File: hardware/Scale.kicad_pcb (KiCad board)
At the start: 2 copper layers, 45 x 45 mm, 158 parts, among them J1 Load Cell Connector, J2 GPIO, J3 RS232, J4 DebugEdge_02x03, J5 Display Connector, J7 12401610E4#2A, Q1 DMG2307L, Q2 DMG2307L, Q3 BSD235N, SW1 RESET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

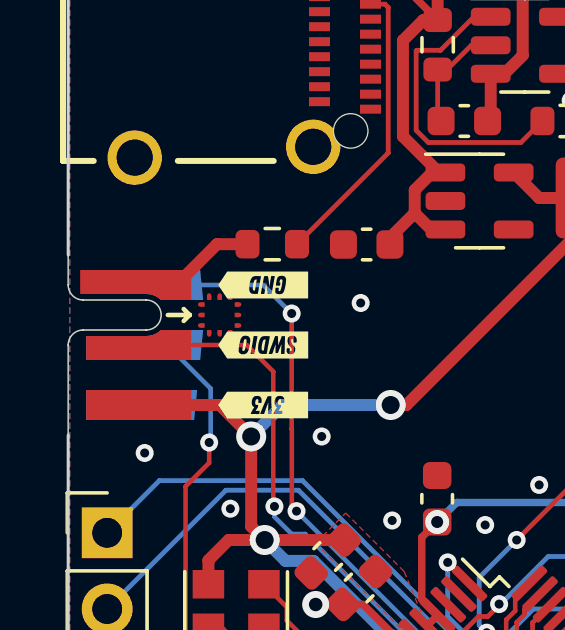
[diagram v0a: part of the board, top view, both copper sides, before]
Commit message: Fixed encoder and usb 3D models
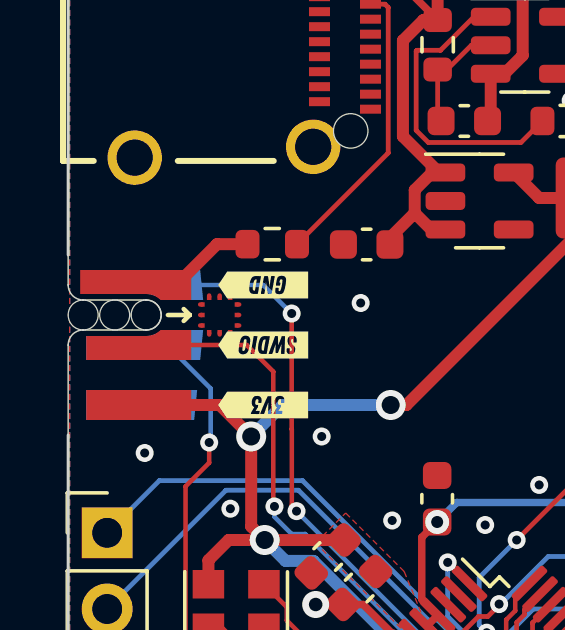
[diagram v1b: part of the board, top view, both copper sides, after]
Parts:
- added REF**: NPTH, PCM_kikit:NPTH, F.Cu at (115.8, 62.6)
- added REF**: NPTH, PCM_kikit:NPTH, F.Cu at (114.8, 62.6)
- added REF**: NPTH, PCM_kikit:NPTH, F.Cu at (113.8, 62.6)
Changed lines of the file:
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@@
 		)
 	)
+	(footprint "PCM_kikit:NPTH"
+		(layer "F.Cu")
+		(at 115.85 62.65)
+		(property "Reference" "REF**"
+			(at 0 0.5 0)
+			(layer "F.SilkS")
+			(hide yes)
+			(effects
+				(font
+					(size 1 1)
+					(thickness 0.15)
+				)
+			)
+		)
+		(property "Value" "NPTH"
+			(at 0 -0.5 0)
+			(layer "F.Fab")
+			(hide yes)
+			(effects
+				(font
+					(size 1 1)
+					(thickness 0.15)
+				)
+			)
+		)
+		(property "Datasheet" ""
+			(at 0 0 0)
+			(layer "F.Fab")
+			(hide yes)
+			(effects
+				(font
+					(size 1.27 1.27)
+					(thickness 0.15)
+				)
+			)
+		)
+		(property "Description" ""
+			(at 0 0 0)
+			(layer "F.Fab")
+			(hide yes)
+			(effects
+				(font
+					(size 1.27 1.27)
+					(thickness 0.15)
+				)
+			)
+		)
+		(attr through_hole)
+		(pad "" np_thru_hole circle
+			(at 0 0)
+			(size 1 1)
+			(drill 1)
+			(layers "*.Mask")
+		)
+		(embedded_fonts no)
+	)
 	(footprint "Resistor_SMD:R_0603_1608Metric"
 		(placed yes)
@@
 		)
 	)
+	(footprint "PCM_kikit:NPTH"
+		(layer "F.Cu")
+		(at 114.8 62.65)
+		(property "Reference" "REF**"
+			(at 0 0.5 0)
+			(layer "F.SilkS")
+			(hide yes)
+			(effects
+				(font
+					(size 1 1)
+					(thickness 0.15)
+				)
+			)
+		)
+		(property "Value" "NPTH"
+			(at 0 -0.5 0)
+			(layer "F.Fab")
+			(hide yes)
+			(effects
+				(font
+					(size 1 1)
+					(thickness 0.15)
+				)
+			)
+		)
+		(property "Datasheet" ""
+			(at 0 0 0)
+			(layer "F.Fab")
+			(hide yes)
+			(effects
+				(font
+					(size 1.27 1.27)
+					(thickness 0.15)
+				)
+			)
+		)
+		(property "Description" ""
+			(at 0 0 0)
+			(layer "F.Fab")
+			(hide yes)
+			(effects
+				(font
+					(size 1.27 1.27)
+					(thickness 0.15)
+				)
+			)
+		)
+		(attr through_hole)
+		(pad "" np_thru_hole circle
+			(at 0 0)
+			(size 1 1)
+			(drill 1)
+			(layers "*.Mask")
+		)
+		(embedded_fonts no)
+	)
 	(footprint "Resistor_SMD:R_0603_1608Metric"
 		(placed yes)
@@
 		)
 	)
+	(footprint "PCM_kikit:NPTH"
+		(layer "F.Cu")
+		(at 113.75 62.65)
+		(property "Reference" "REF**"
+			(at 0 0.5 0)
+			(layer "F.SilkS")
+			(hide yes)
+			(effects
+				(font
+					(size 1 1)
+					(thickness 0.15)
+				)
+			)
+		)
+		(property "Value" "NPTH"
+			(at 0 -0.5 0)
+			(layer "F.Fab")
+			(hide yes)
+			(effects
+				(font
+					(size 1 1)
+					(thickness 0.15)
+				)
+			)
+		)
+		(property "Datasheet" ""
+			(at 0 0 0)
+			(layer "F.Fab")
+			(hide yes)
+			(effects
+				(font
+					(size 1.27 1.27)
+					(thickness 0.15)
+				)
+			)
+		)
+		(property "Description" ""
+			(at 0 0 0)
+			(layer "F.Fab")
+			(hide yes)
+			(effects
+				(font
+					(size 1.27 1.27)
+					(thickness 0.15)
+				)
+			)
+		)
+		(attr through_hole)
+		(pad "" np_thru_hole circle
+			(at 0 0)
+			(size 1 1)
+			(drill 1)
+			(layers "*.Mask")
+		)
+		(embedded_fonts no)
+	)
 	(footprint "Package_TO_SOT_SMD:SOT-363_SC-70-6"
 		(layer "F.Cu")
@@
 		)
 		(embedded_fonts no)
-		(model "PEC12R-3217F-S0024.stp"
+		(model "/home/benjamin/Projects/common/kicad_libraries/3d/PEC12R-4120F-S0012.stp"
 			(offset
-				(xyz 2.499999962 -6.999999895 -1.049999937)
+				(xyz 2.5 -7 0)
 			)
 			(scale
@@
 			)
 			(rotate
-				(xyz 0 0 90)
+				(xyz -90 -0 -180)
 			)
 		)
@@
 		)
 		(embedded_fonts no)
-		(model "12401610E4#2A.stp"
+		(model "/home/benjamin/Projects/common/kicad_libraries/3d/12401610E4#2A.stp"
 			(offset
-				(xyz 0.1099999978 -5.15999977 1.529999948)
+				(xyz 0.125 -5.225 1.5)
 			)
 			(scale
@@
 			)
 			(rotate
-				(xyz 0 0 90)
+				(xyz -0 -0 90)
 			)
 		)
